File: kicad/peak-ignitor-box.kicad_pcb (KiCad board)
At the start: 4 copper layers, 91 x 56 mm, 141 parts, among them J1 +24V, J10 SW, J11 Conn_01x01, J12 Conn_01x01, J13 Conn_01x01, J14 Conn_01x01, J15 GND, J2 GND, J3 PROG, J4 JTAG, J5 BATT, J6 GND, J7 +12V, J9 BATT-sw, Q1 BSS138, Q2 BSS138, Q3 IRLML9301, Q4 NVTFS5C454NLWFTAG, Q5 NVTFS5C454NLWFTAG, Q6 NVTFS5C454NLWFTAG, Q7 NVTFS5C454NLWFTAG, Q8 NVTFS5C454NLWFTAG, Q9 NVTFS5C454NLWFTAG, SW1 GT-TC029B-H025-L1N, SW2 GT-TC029B-H025-L1N, U1 TMP1075, U2 TMP1075, U3 ESP32-S3-MINI-1, U4 BQ24600, U5 AP3211, U6 LM51770DCPR

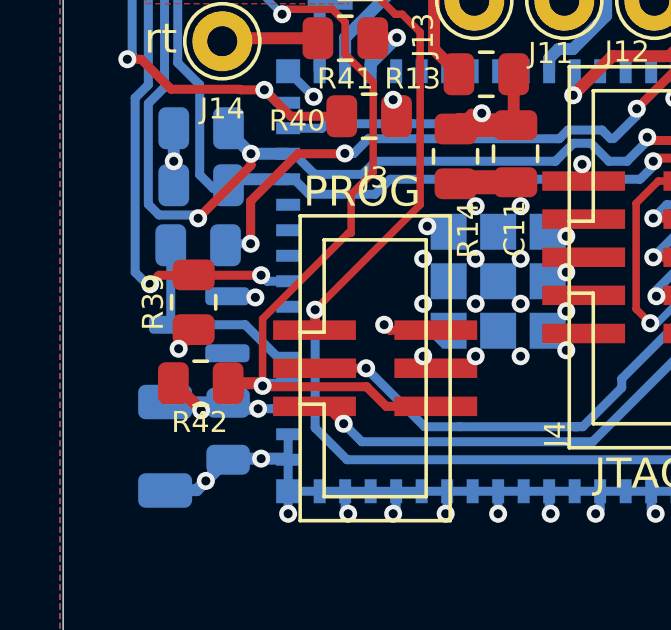
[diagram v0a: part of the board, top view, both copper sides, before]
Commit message: updated gerbers, bom, some bug fixes on schematic and board
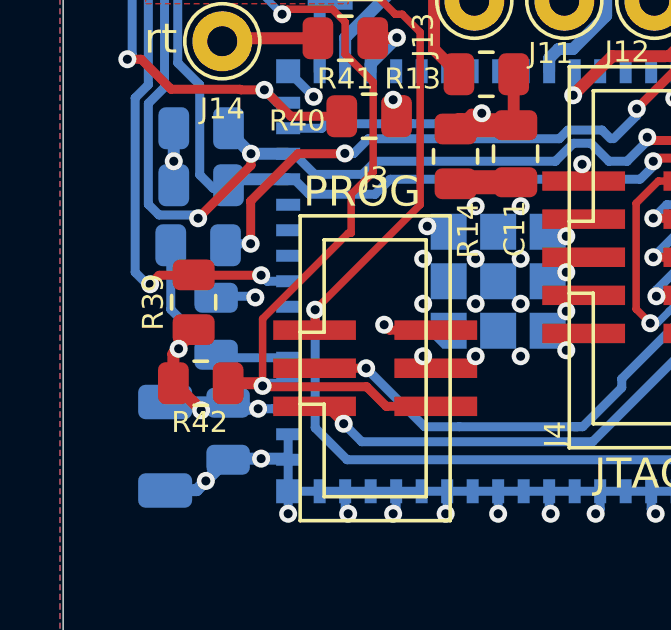
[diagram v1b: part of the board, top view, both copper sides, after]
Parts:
- removed D6: BZX84C3V3, Package_TO_SOT_SMD:SOT-23
- added C24: 100n, Capacitor_SMD:C_0805_2012Metric, B.Cu at (202.1, 118.1)
- R13: value 102k -> 100k
- R14: value 24.3k -> 20k
- R6: value 22.1k -> 12k
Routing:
- net +3V3: track 61.5 -> 62.7 mm

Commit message: added 160W discharge
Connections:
- R1 pad 2: LED_RED -> LED_GREEN
- R41 pad 2: LED_GREEN -> LED_RED
- U3 pad 18: LED_GREEN -> LED_RED
- U3 pad 26: LED_RED -> LED_GREEN
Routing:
- net LED_RED: track 9.07 -> 2.30 mm
- net LED_GREEN: track 2.30 -> 9.07 mm
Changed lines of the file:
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@@
 			(layers "F.Cu" "F.Mask" "F.Paste")
 			(roundrect_rratio 0.243902)
-			(net 102 "LED_GREEN")
+			(net 101 "LED_RED")
 			(pintype "passive")
 		)
@@
 			(layers "F.Cu" "F.Mask" "F.Paste")
 			(roundrect_rratio 0.243902)
-			(net 101 "LED_RED")
+			(net 102 "LED_GREEN")
 			(pintype "passive")
 		)
@@
 		(sheetname "/")
 		(sheetfile "peak-ignitor-box.kicad_sch")
-		(attr through_hole)
+		(attr through_hole dnp)
 		(fp_line
 			(start -2.5 -6.35)
@@
 		(sheetname "/")
 		(sheetfile "peak-ignitor-box.kicad_sch")
-		(attr smd)
+		(attr smd dnp)
 		(fp_line
 			(start -2.2 -1.55)
@@
 		(sheetname "/")
 		(sheetfile "peak-ignitor-box.kicad_sch")
-		(attr smd)
+		(attr smd dnp)
 		(fp_line
 			(start 2.2 1.55)
@@
 			(size 0.8 0.4)
 			(layers "B.Cu" "B.Mask" "B.Paste")
-			(net 102 "LED_GREEN")
+			(net 101 "LED_RED")
 			(pinfunction "IO14")
 			(pintype "bidirectional")
@@
 			(size 0.8 0.4)
 			(layers "B.Cu" "B.Mask" "B.Paste")
-			(net 101 "LED_RED")
+			(net 102 "LED_GREEN")
 			(pinfunction "IO26")
 			(pintype "bidirectional")
@@
 	)
 	(segment
-		(start 219.705 108.2)
-		(end 220.8175 107.0875)
+		(start 208.105 108.5)
+		(end 208.125202 108.479798)
 		(width 0.4)
 		(layer "F.Cu")
@@
 	)
 	(segment
-		(start 220.8175 107.0875)
-		(end 220.8175 106.9)
+		(start 207.3175 108.5)
+		(end 208.105 108.5)
 		(width 0.4)
 		(layer "F.Cu")
 		(net 101)
 	)
+	(via
+		(at 208.125202 108.479798)
+		(size 0.6)
+		(drill 0.3)
+		(layers "F.Cu" "B.Cu")
+		(net 101)
+	)
 	(segment
-		(start 217.205 109.1)
-		(end 218.105 108.2)
+		(start 207.25 109.355)
+		(end 208.125202 108.479798)
 		(width 0.4)
-		(layer "F.Cu")
+		(layer "B.Cu")
 		(net 101)
 	)
 	(segment
-		(start 218.105 108.2)
-		(end 219.705 108.2)
+		(start 207.25 109.6)
+		(end 207.25 109.355)
 		(width 0.4)
-		(layer "F.Cu")
+		(layer "B.Cu")
 		(net 101)
 	)
 	(segment
-		(start 215.3 109.1)
-		(end 214 110.4)
+		(start 219.705 108.2)
+		(end 220.8175 107.0875)
 		(width 0.4)
 		(layer "F.Cu")
-		(net 101)
+		(net 102)
 	)
 	(segment
-		(start 217.075763 109.1)
-		(end 215.3 109.1)
+		(start 220.8175 107.0875)
+		(end 220.8175 106.9)
 		(width 0.4)
 		(layer "F.Cu")
-		(net 101)
-	)
-	(via
-		(at 214 110.4)
-		(size 0.6)
-		(drill 0.3)
-		(layers "F.Cu" "B.Cu")
-		(net 101)
+		(net 102)
 	)
 	(segment
-		(start 214.05 110.35)
-		(end 214 110.4)
+		(start 217.205 109.1)
+		(end 218.105 108.2)
 		(width 0.4)
-		(layer "B.Cu")
-		(net 101)
+		(layer "F.Cu")
+		(net 102)
 	)
 	(segment
-		(start 214.05 109.6)
-		(end 214.05 110.35)
+		(start 218.105 108.2)
+		(end 219.705 108.2)
 		(width 0.4)
-		(layer "B.Cu")
-		(net 101)
+		(layer "F.Cu")
+		(net 102)
 	)
 	(segment
-		(start 208.105 108.5)
-		(end 208.125202 108.479798)
+		(start 215.3 109.1)
+		(end 214 110.4)
 		(width 0.4)
 		(layer "F.Cu")
@@
 	)
 	(segment
-		(start 207.3175 108.5)
-		(end 208.105 108.5)
+		(start 217.075763 109.1)
+		(end 215.3 109.1)
 		(width 0.4)
 		(layer "F.Cu")
@@
 	)
 	(via
-		(at 208.125202 108.479798)
+		(at 214 110.4)
 		(size 0.6)
 		(drill 0.3)
@@
 	)
 	(segment
-		(start 207.25 109.355)
-		(end 208.125202 108.479798)
+		(start 214.05 110.35)
+		(end 214 110.4)
 		(width 0.4)
 		(layer "B.Cu")
@@
 	)
 	(segment
-		(start 207.25 109.6)
-		(end 207.25 109.355)
+		(start 214.05 109.6)
+		(end 214.05 110.35)
 		(width 0.4)
 		(layer "B.Cu")

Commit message: rev1.1
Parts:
- added C46: 10µ/35V, Capacitor_SMD:C_1210_3225Metric, F.Cu at (255.4, 90.0)
- added D6: SMCJ15A, Diode_SMD:D_SMC, F.Cu at (262.3, 90.7)
- added REF**: OSHW-Logo2_9.8x8mm_SilkScreen, Symbol:OSHW-Logo2_9.8x8mm_SilkScreen, F.Cu at (282.6, 105.3)
- added REF**: KiCad-Logo2_5mm_SilkScreen, Symbol:KiCad-Logo2_5mm_SilkScreen, F.Cu at (283.0, 122.0)
- NT5: moved to B.Cu
- moved R34 11.3 mm to (249.0, 93.4), turned to -90 degrees
- moved R33 8.19 mm to (247.1, 93.4), turned to 90 degrees
- moved NT5 6.10 mm to (250.4, 94.0)
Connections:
- F3 pad 1: Net-(F3-Pad1) -> Net-(C46-Pad1)
- NT4 pad 2: Net-(F3-Pad1) -> Net-(C46-Pad1)
- NT5 pad 2: Net-(Q8-D) -> Net-(C46-Pad1)
- R33 pad 1: Net-(Q8-D) -> Net-(C46-Pad1)
- R35 pad 2: Net-(F3-Pad1) -> Net-(C46-Pad1)
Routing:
- net Net-(C46-Pad1): track 0.00 -> 16.6 mm, vias 0 -> 12
- net GND: track 141.9 -> 152.2 mm, vias 239 -> 242
- net Net-(U6-FB): track 19.1 -> 10.5 mm
- net Net-(U6-VOUT): track 20.6 -> 14.5 mm, vias 1 -> 0
- net Net-(D6-A1): track 0.00 -> 6.01 mm
- net Net-(Q8-D): track 5.41 -> 2.22 mm
- net Net-(F3-Pad1): track 2.12 -> 0.00 mm, vias 11 -> 0
- added copper zone on B.Cu, net Net-(C46-Pad1)
- added copper zone on F.Cu, net Net-(C46-Pad1)
- added copper zone on In1.Cu, net Net-(C46-Pad1)
- removed copper zone on B.Cu, net Net-(F3-Pad1)
- removed copper zone on F.Cu, net Net-(F3-Pad1)
- removed copper zone on In1.Cu, net Net-(F3-Pad1)
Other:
- board size 91 x 56 mm -> 91 x 57 mm
- board text added: "V1.1"
- board text removed: "V1.0"

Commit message: push
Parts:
- removed NT5: NetTie_2, NetTie:NetTie-2_SMD_Pad0.5mm
- moved R34 103.5 mm to (145.5, 90.4), turned to 90 degrees
- moved R33 101.6 mm to (145.5, 93.9)
- moved C11 97.4 mm to (114.9, 106.2)
- moved C17 97.4 mm to (113.8, 85.7)
- moved C25 97.4 mm to (147.6, 86.7)
- moved C27 97.4 mm to (145.6, 86.7)
- moved C29 97.4 mm to (143.6, 86.7)
- moved C30 97.4 mm to (139.5, 99.2)
- moved C31 97.4 mm to (134.1, 86.8)
- moved C32 97.4 mm to (133.1, 97.8)
- moved C34 97.4 mm to (133.1, 101.0)
- moved C39 97.4 mm to (133.4, 97.3)
- moved C43 97.4 mm to (152.6, 101.0)
- moved C44 97.4 mm to (145.3, 90.7)
- moved C46 97.4 mm to (158.2, 83.9)
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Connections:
- C46 pad 1: Net-(C46-Pad1) -> Net-(U6-VOUT)
- F3 pad 1: Net-(C46-Pad1) -> Net-(U6-VOUT)
- NT4 pad 2: Net-(C46-Pad1) -> Net-(U6-VOUT)
- R33 pad 1: Net-(C46-Pad1) -> Net-(U6-VOUT)
- R35 pad 2: Net-(C46-Pad1) -> Net-(U6-VOUT)
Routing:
- net Net-(C46-Pad1): track 16.6 -> 0.00 mm, vias 12 -> 0
- net Net-(U6-VOUT): track 14.5 -> 29.1 mm, vias 0 -> 11
- net Net-(U6-FB): track 10.5 -> 3.75 mm
- added copper zone on B.Cu, net Net-(U6-VOUT)
- added copper zone on F.Cu, net Net-(U6-VOUT)
- added copper zone on In1.Cu, net Net-(U6-VOUT)
- removed copper zone on B.Cu, net Net-(C46-Pad1)
- removed copper zone on F.Cu, net Net-(C46-Pad1)
- removed copper zone on In1.Cu, net Net-(C46-Pad1)
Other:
- board size 91 x 57 mm -> 90.5 x 57 mm
